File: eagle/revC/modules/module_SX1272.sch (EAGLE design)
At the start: 18 parts, among them X1 734120110

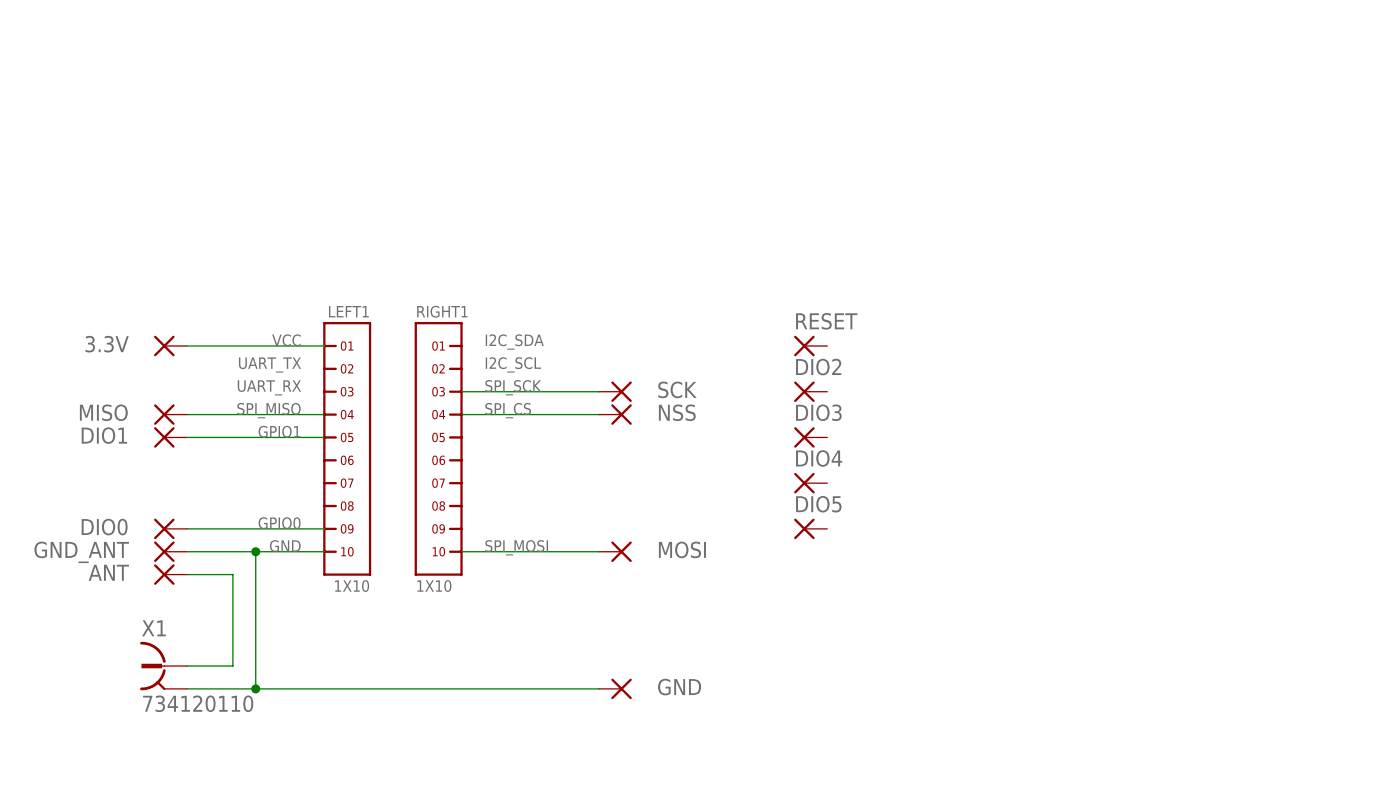
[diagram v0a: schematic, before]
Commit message: Replaced modules with library parts
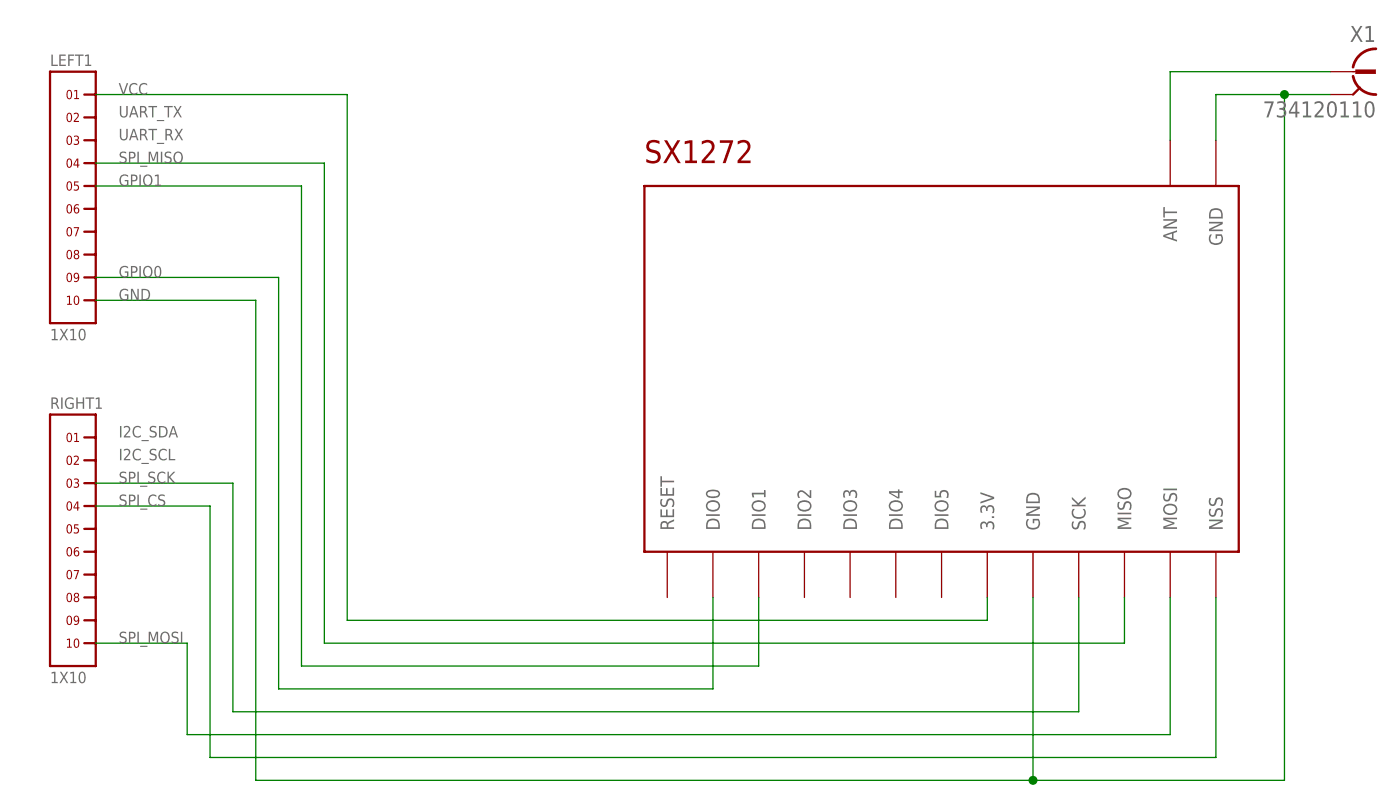
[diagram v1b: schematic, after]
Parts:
- removed 3.3V, ANT, DIO0, DIO1, DIO2, DIO3, DIO4, DIO5, GND, GND_ANT, MISO, MOSI, NSS, RESET, SCK: (no value), wirepad:SMD1
- added U$1: SX1272, RadioShield:SX1272
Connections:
- removed net ANT: ANT.P, X1.1
- removed net INT0: DIO0.P, LEFT1.9
- removed net INT1: DIO1.P, LEFT1.5
- removed net SPI_CS: NSS.P, RIGHT1.4
- removed net SPI_MISO: LEFT1.4, MISO.P
- removed net SPI_MOSI: MOSI.P, RIGHT1.10
- removed net SPI_SCK: RIGHT1.3, SCK.P
- new net N$2: U$1.ANT, X1.1
- new net N$3: LEFT1.9, U$1.DIO0
- new net N$4: RIGHT1.10, U$1.MOSI
- new net N$5: RIGHT1.4, U$1.NSS
- new net N$6: RIGHT1.3, U$1.SCK
- new net N$7: LEFT1.5, U$1.DIO1
- new net N$8: LEFT1.4, U$1.MISO
- net GND: now also U$1.GND@1, U$1.GND@2; no longer GND.P, GND_ANT.P
- net VCC: now also U$1.3.3V; no longer 3.3V.P
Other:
- moved on the sheet: LEFT1, RIGHT1, X1
